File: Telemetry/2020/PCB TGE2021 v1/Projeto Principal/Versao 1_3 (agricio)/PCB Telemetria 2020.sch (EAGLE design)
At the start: 39 parts, among them IC1 INA240A1DR, IC2 MCP3221A6T-E_OTVAO, IC3 AZ1117IH-3.3TRG1, IC4 ACS758LCB-050B-PFF-T, IC5 ADS1115IDGSR, U2 ACS712ELCTR-05B-T

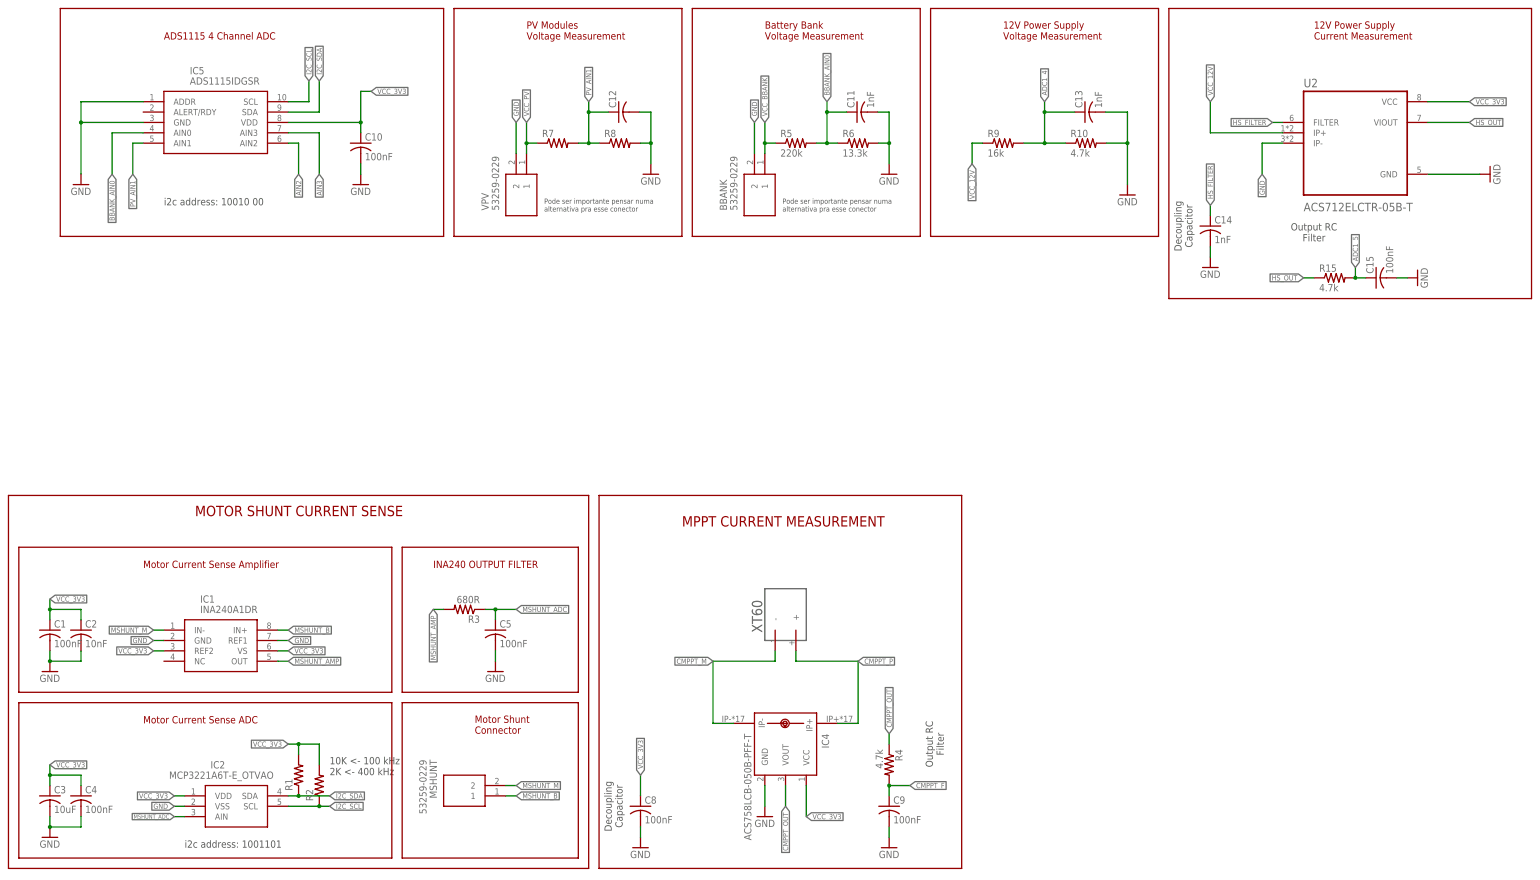
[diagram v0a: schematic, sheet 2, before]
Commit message: Correcao no circuito de medicao de corrente, adicao de conectores e simulacao da medicao de corrente
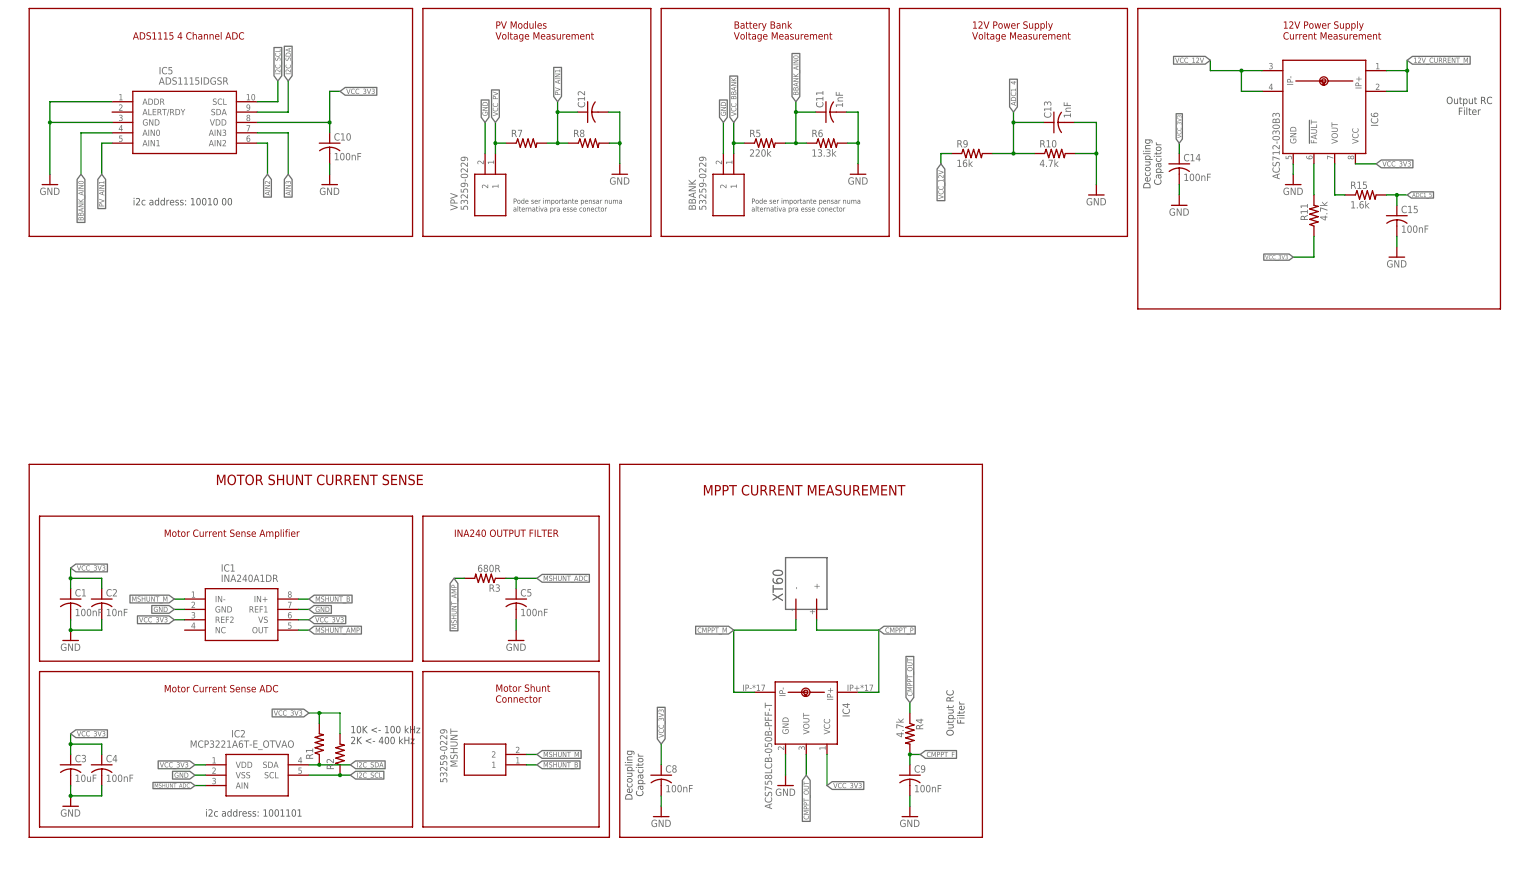
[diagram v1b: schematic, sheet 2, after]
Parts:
- removed 12V_POWER: 43650-0200, 43650-0200:43650-0200
- removed U2: ACS712ELCTR-05B-T, ACS712ELCTR-05B-T:ACS712ELCTR-05B-T
- added IC6: ACS712-030B3, allegro-2:ACS712-LC
- added J1: 172042-0406, 172042-0302:172042-0406
- added R11: 4.7k, rcl:R-US_R0805
- C14: value 1nF -> 100nF
- R15: value 4.7k -> 1.6k
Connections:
- removed net HS_FILTER: C14.1, U2.FILTER
- removed net HS_OUT: R15.1, U2.VIOUT
- new net 12V_CURRENT_M: IC6.IP+, IC6.IP+1, J1.3
- new net N$1: IC6.!FAULT, R11.2
- new net N$2: IC6.VOUT, R15.1
- net GND: now also IC6.GND, J1.1; no longer 12V_POWER.1, U2.GND, U2.IP-
- net VCC_12V: now also IC6.IP-, IC6.IP-1, J1.2; no longer 12V_POWER.2, U2.IP+
- net VCC_3V3: now also C14.1, IC6.VCC, R11.1; no longer U2.VCC
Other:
- moved on the sheet: BBANK, C1, C10, C11, C12, C13, C14, C15, C2, C3, C4, C5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
